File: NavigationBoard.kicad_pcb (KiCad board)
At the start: 2 copper layers, 50 x 45 mm, 49 parts, among them J1 Conn_01x03, J2 Conn_01x03, J3 Conn_01x03, J4 Conn_01x03, J5 USB_C_Receptacle_USB2.0, J6 AVR-ISP-6, J7 Conn_01x02, SW1 SW_Push, U1 ATmega2560-16AU, U2 RFM96W-433S2, U3 FT230XQ, U4 MPL3115A2, U5 ublox_SAM-M8Q, U6 LMZM23600V3, Y1 16MHz

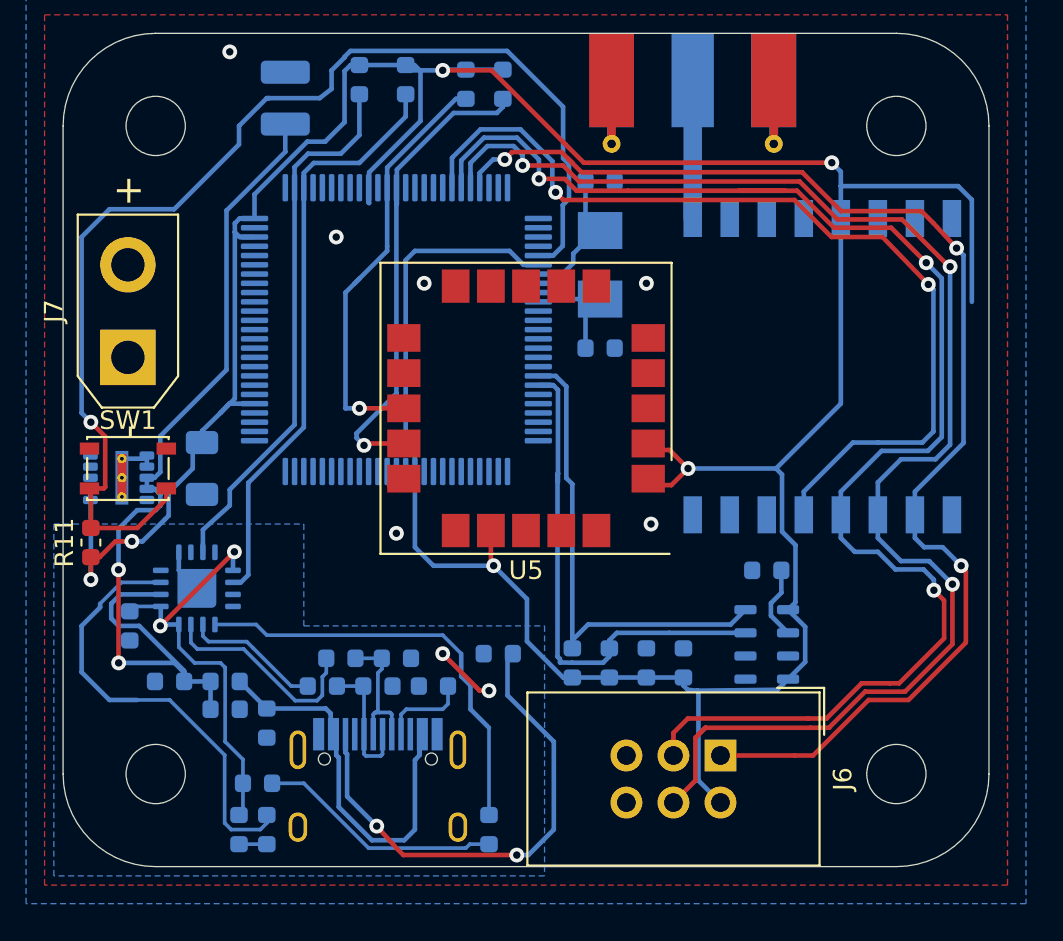
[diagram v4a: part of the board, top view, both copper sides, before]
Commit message: Kleinerer AVR-ISP Stecker
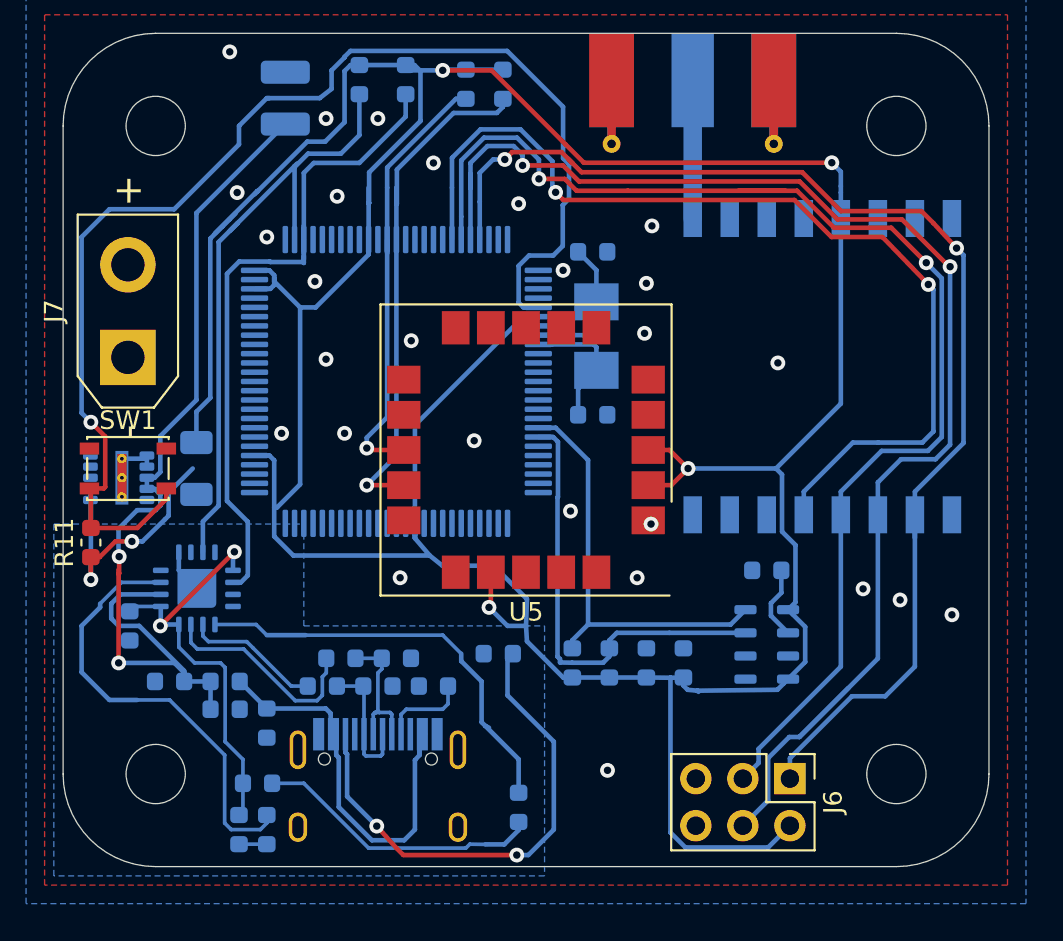
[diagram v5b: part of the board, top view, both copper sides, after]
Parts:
- J6: footprint Connector_IDC:IDC-Header_2x03_P2.54mm_Vertical -> Connector_PinHeader_2.54mm:PinHeader_2x03_P2.54mm_Vertical
- moved J6 3.95 mm to (39.2, 40.2)
- moved Y1 3.86 mm to (28.8, 16.4)
- moved C8 3.82 mm to (28.6, 11.8)
- moved C7 3.62 mm to (28.6, 20.6)
- moved U1 2.80 mm to (18.0, 18.8)
- moved U5 2.25 mm to (25.0, 22.5)
- moved D2 2.00 mm to (24.6, 41.8)
- moved C10 0.30 mm to (7.20, 23.5)
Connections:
- J1 pad 1: Net-(J1-Pad1) -> (no net)
- J1 pad 2: Net-(J1-Pad2) -> (no net)
- J1 pad 3: Net-(J1-Pad3) -> (no net)
- J2 pad 1: Net-(J2-Pad1) -> (no net)
- J2 pad 2: Net-(J2-Pad2) -> (no net)
- J2 pad 3: Net-(J2-Pad3) -> (no net)
- J3 pad 1: Net-(J3-Pad1) -> (no net)
- J3 pad 2: Net-(J3-Pad2) -> (no net)
- J3 pad 3: Net-(J3-Pad3) -> (no net)
- J4 pad 1: Net-(J4-Pad1) -> (no net)
- J4 pad 2: Net-(J4-Pad2) -> (no net)
- J4 pad 3: Net-(J4-Pad3) -> (no net)
- J5 pad A8: Net-(J5-PadA8) -> (no net)
- J5 pad B8: Net-(J5-PadB8) -> (no net)
- J6 pad 5: /~RST -> (no net)
- J7 pad 1: Net-(J7-Pad1) -> (no net)
- J7 pad 2: Net-(J7-Pad2) -> (no net)
- U1 pad 1: Net-(U1-Pad1) -> (no net)
- U1 pad 14: Net-(U1-Pad14) -> (no net)
- U1 pad 15: Net-(U1-Pad15) -> (no net)
- U1 pad 16: Net-(U1-Pad16) -> (no net)
- U1 pad 17: Net-(U1-Pad17) -> (no net)
- U1 pad 18: Net-(U1-Pad18) -> (no net)
- U1 pad 23: Net-(U1-Pad23) -> (no net)
- U1 pad 24: Net-(U1-Pad24) -> (no net)
- U1 pad 25: Net-(U1-Pad25) -> (no net)
- U1 pad 26: Net-(U1-Pad26) -> (no net)
- U1 pad 27: Net-(U1-Pad27) -> (no net)
- U1 pad 28: Net-(U1-Pad28) -> (no net)
- U1 pad 29: Net-(U1-Pad29) -> (no net)
- U1 pad 35: Net-(U1-Pad35) -> (no net)
- U1 pad 36: Net-(U1-Pad36) -> (no net)
- U1 pad 37: Net-(U1-Pad37) -> (no net)
- U1 pad 38: Net-(U1-Pad38) -> (no net)
- U1 pad 39: Net-(U1-Pad39) -> (no net)
- U1 pad 4: Net-(U1-Pad4) -> (no net)
- U1 pad 40: Net-(U1-Pad40) -> (no net)
- U1 pad 41: Net-(U1-Pad41) -> (no net)
- U1 pad 42: Net-(U1-Pad42) -> (no net)
- U1 pad 45: Net-(U1-Pad45) -> (no net)
- U1 pad 46: Net-(U1-Pad46) -> (no net)
- U1 pad 47: Net-(U1-Pad47) -> (no net)
- U1 pad 48: Net-(U1-Pad48) -> (no net)
- U1 pad 49: Net-(U1-Pad49) -> (no net)
- U1 pad 5: Net-(U1-Pad5) -> (no net)
- U1 pad 50: Net-(U1-Pad50) -> (no net)
- U1 pad 51: Net-(U1-Pad51) -> (no net)
- U1 pad 52: Net-(U1-Pad52) -> (no net)
- U1 pad 53: Net-(U1-Pad53) -> (no net)
- U1 pad 54: Net-(U1-Pad54) -> (no net)
- U1 pad 55: Net-(U1-Pad55) -> (no net)
- U1 pad 56: Net-(U1-Pad56) -> (no net)
- U1 pad 57: Net-(U1-Pad57) -> (no net)
- U1 pad 58: Net-(U1-Pad58) -> (no net)
- U1 pad 59: Net-(U1-Pad59) -> (no net)
- U1 pad 6: Net-(U1-Pad6) -> (no net)
- U1 pad 60: Net-(U1-Pad60) -> (no net)
- U1 pad 63: Net-(U1-Pad63) -> (no net)
- U1 pad 64: Net-(U1-Pad64) -> (no net)
- U1 pad 65: Net-(U1-Pad65) -> (no net)
- U1 pad 66: Net-(U1-Pad66) -> (no net)
- U1 pad 67: Net-(U1-Pad67) -> (no net)
- U1 pad 68: Net-(U1-Pad68) -> (no net)
- U1 pad 69: Net-(U1-Pad69) -> (no net)
- U1 pad 7: Net-(U1-Pad7) -> (no net)
- U1 pad 70: Net-(U1-Pad70) -> (no net)
- U1 pad 71: Net-(U1-Pad71) -> (no net)
- U1 pad 72: Net-(U1-Pad72) -> (no net)
- U1 pad 73: Net-(U1-Pad73) -> (no net)
- U1 pad 74: Net-(U1-Pad74) -> (no net)
- U1 pad 75: Net-(U1-Pad75) -> (no net)
- U1 pad 76: Net-(U1-Pad76) -> (no net)
- U1 pad 77: Net-(U1-Pad77) -> (no net)
- U1 pad 78: Net-(U1-Pad78) -> (no net)
- U1 pad 79: Net-(U1-Pad79) -> (no net)
- U1 pad 8: Net-(U1-Pad8) -> (no net)
- U1 pad 82: Net-(U1-Pad82) -> (no net)
- U1 pad 83: Net-(U1-Pad83) -> (no net)
- U1 pad 84: Net-(U1-Pad84) -> (no net)
- U1 pad 85: Net-(U1-Pad85) -> (no net)
- U1 pad 86: Net-(U1-Pad86) -> (no net)
- U1 pad 87: Net-(U1-Pad87) -> (no net)
- U1 pad 88: Net-(U1-Pad88) -> (no net)
- U1 pad 89: Net-(U1-Pad89) -> (no net)
- U1 pad 9: Net-(U1-Pad9) -> (no net)
- U1 pad 90: Net-(U1-Pad90) -> (no net)
- U1 pad 91: Net-(U1-Pad91) -> (no net)
- U1 pad 92: Net-(U1-Pad92) -> (no net)
- U1 pad 93: Net-(U1-Pad93) -> (no net)
- U1 pad 94: Net-(U1-Pad94) -> (no net)
- U1 pad 95: Net-(U1-Pad95) -> (no net)
- U1 pad 96: Net-(U1-Pad96) -> (no net)
- U1 pad 97: Net-(U1-Pad97) -> (no net)
- U2 pad 11: Net-(U2-Pad11) -> (no net)
- U2 pad 12: Net-(U2-Pad12) -> (no net)
- U2 pad 14: Net-(U2-Pad14) -> (no net)
- U2 pad 15: Net-(U2-Pad15) -> (no net)
- U2 pad 16: Net-(U2-Pad16) -> (no net)
- U2 pad 6: Net-(U2-Pad6) -> (no net)
- U2 pad 7: Net-(U2-Pad7) -> (no net)
- U3 pad 12: Net-(U3-Pad12) -> (no net)
- U3 pad 14: Net-(U3-Pad14) -> (no net)
- U3 pad 16: Net-(U3-Pad16) -> (no net)
- U3 pad 4: Net-(U3-Pad4) -> (no net)
- U4 pad 5: Net-(U4-Pad5) -> (no net)
- U4 pad 6: Net-(U4-Pad6) -> (no net)
- U5 pad 12: Net-(U5-Pad12) -> (no net)
- U5 pad 18: Net-(U5-Pad18) -> (no net)
- U5 pad 19: Net-(U5-Pad19) -> (no net)
- U5 pad 7: Net-(U5-Pad7) -> (no net)
- U5 pad 8: Net-(U5-Pad8) -> (no net)
- U5 pad 9: Net-(U5-Pad9) -> (no net)
- U6 pad 10: Net-(U6-Pad10) -> (no net)
- U6 pad 5: Net-(U6-Pad5) -> (no net)
- U6 pad 8: Net-(U6-Pad8) -> (no net)
- U6 pad 9: Net-(U6-Pad9) -> (no net)
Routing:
- net +3V3: track 196.9 -> 224.2 mm
- net /SCK: track 79.2 -> 69.9 mm, vias 3 -> 2
- net /RXD0: track 29.3 -> 34.1 mm
- net /~RESET: track 64.4 -> 68.8 mm
- net /SDA: track 28.4 -> 24.3 mm
- net /SCL: track 26.5 -> 22.8 mm
- net /MOSI: track 77.5 -> 74.2 mm, vias 3 -> 2
- net GNDS: track 5.74 -> 2.41 mm, vias 2 -> 0
- net /TXD0: track 31.9 -> 35.2 mm
- net /~SS: track 50.3 -> 53.1 mm
- net Net-(D2-Pad2): track 13.3 -> 15.8 mm
- net /MISO: track 69.6 -> 67.3 mm, vias 3 -> 2
- net Net-(D2-Pad1): track 23.3 -> 25.1 mm
- net /RXD2: track 23.2 -> 24.6 mm
- net Net-(C8-Pad1): track 7.80 -> 8.84 mm
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
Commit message: Layout weiter gemacht
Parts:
- moved R8 0.32 mm to (18.4, 2.80)
- moved R7 0.30 mm to (16.0, 2.80)
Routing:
- net +3V3: track 224.2 -> 240.0 mm, vias 6 -> 8
- net /RXD0: track 34.1 -> 39.0 mm
- net /SCK: track 69.9 -> 74.0 mm
- net /~RESET: track 68.8 -> 65.9 mm
- net /~SS: track 53.1 -> 55.9 mm
- net /TXD2: track 29.0 -> 27.8 mm
- net /MOSI: track 74.2 -> 73.0 mm
- net /TXD0: track 35.2 -> 36.1 mm
- net /SDA: track 24.3 -> 23.7 mm
- net GND: vias 27 -> 24

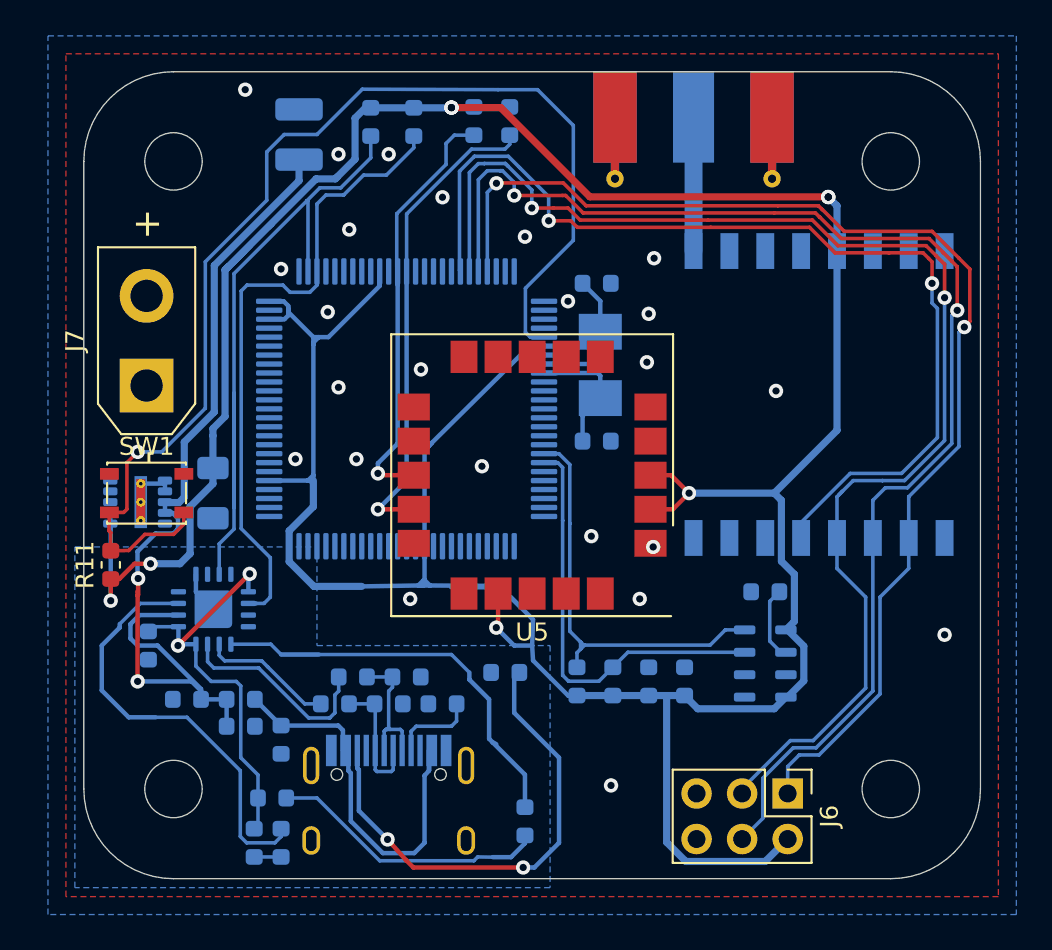
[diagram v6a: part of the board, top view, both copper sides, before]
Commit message: Weniger Leiterbahnen auf der Oberseite
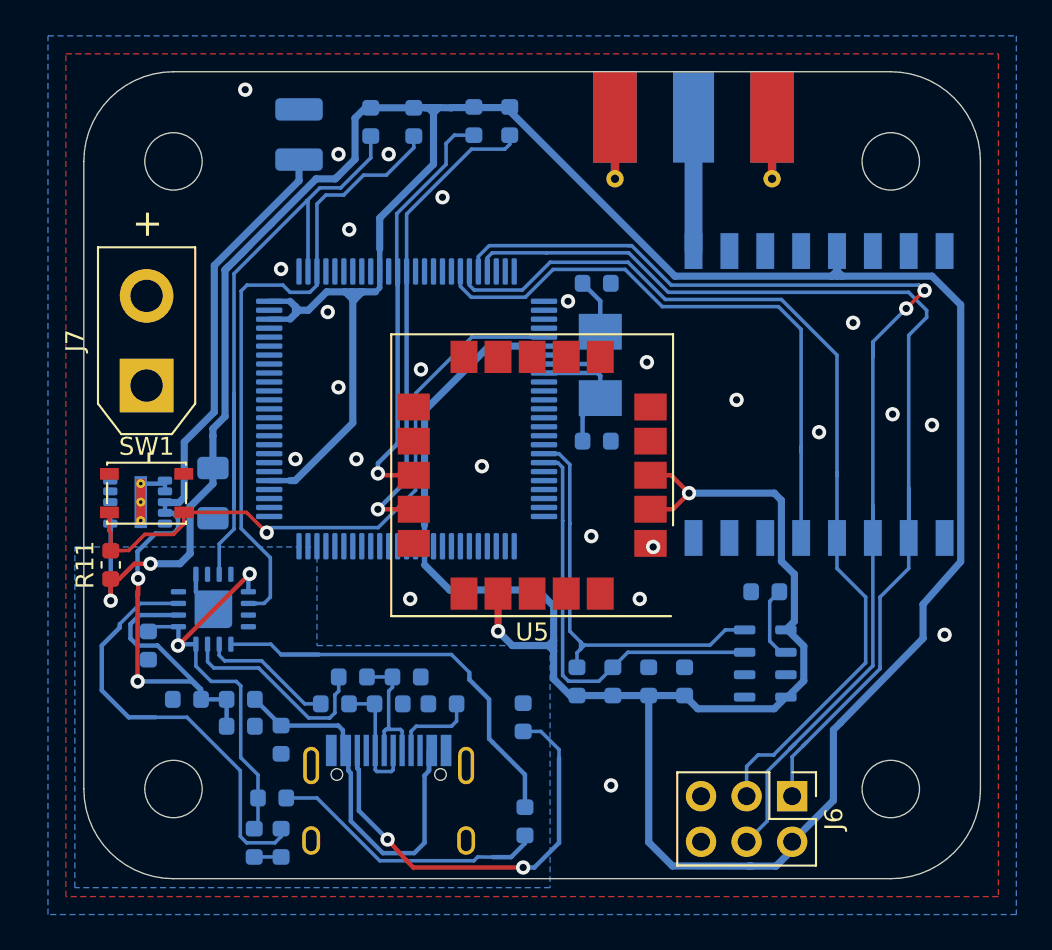
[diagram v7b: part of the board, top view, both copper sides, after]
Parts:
- moved R2 2.69 mm to (24.5, 36.0), turned to 270 degrees
- moved J6 0.29 mm to (39.5, 40.4)
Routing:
- net /~RESET: track 65.9 -> 36.6 mm
- net /~SS: track 55.9 -> 35.0 mm, vias 2 -> 0
- net +3V3: track 240.0 -> 260.4 mm, vias 8 -> 4
- net /SCK: track 74.0 -> 54.0 mm, vias 2 -> 0
- net /MOSI: track 73.0 -> 64.9 mm
- net /MISO: track 67.8 -> 60.1 mm, vias 2 -> 0
- net Net-(J5-PadB5): track 27.1 -> 24.1 mm
- net GND: vias 24 -> 25

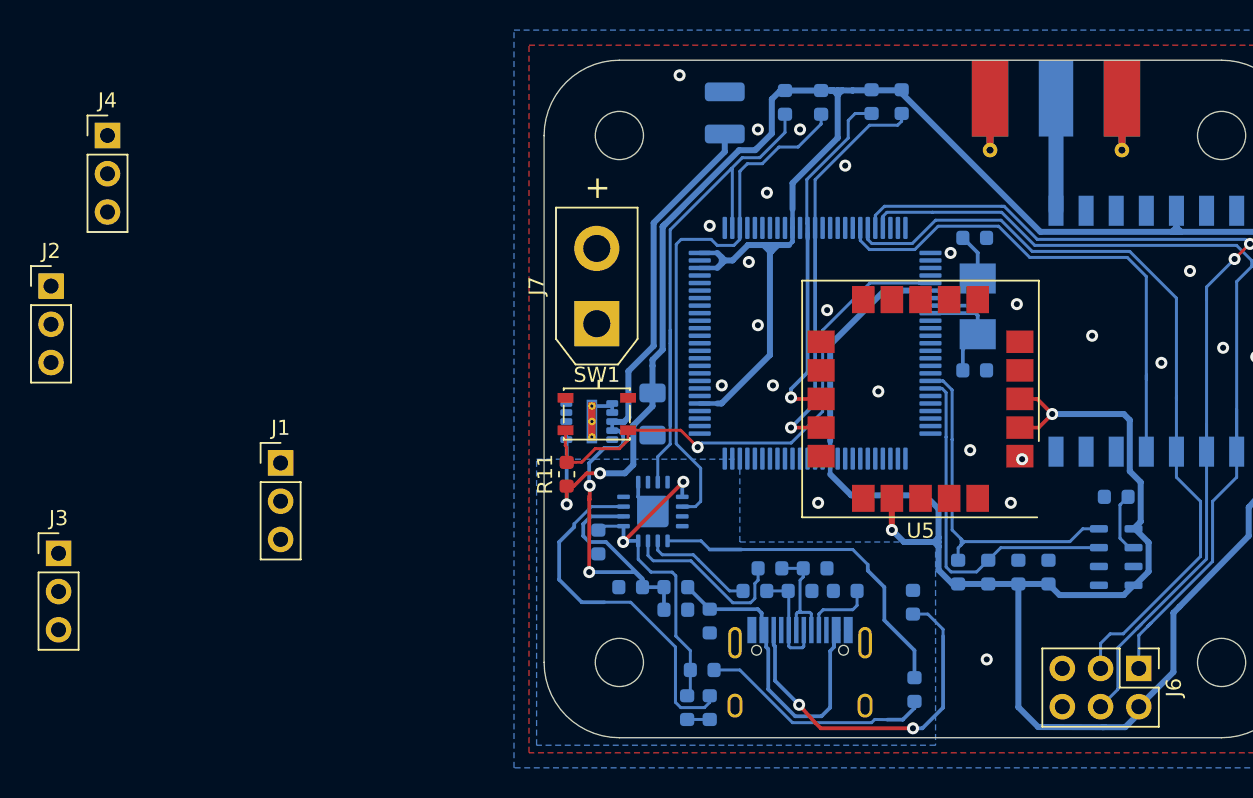
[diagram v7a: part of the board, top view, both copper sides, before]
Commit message: XT 30 entfernt
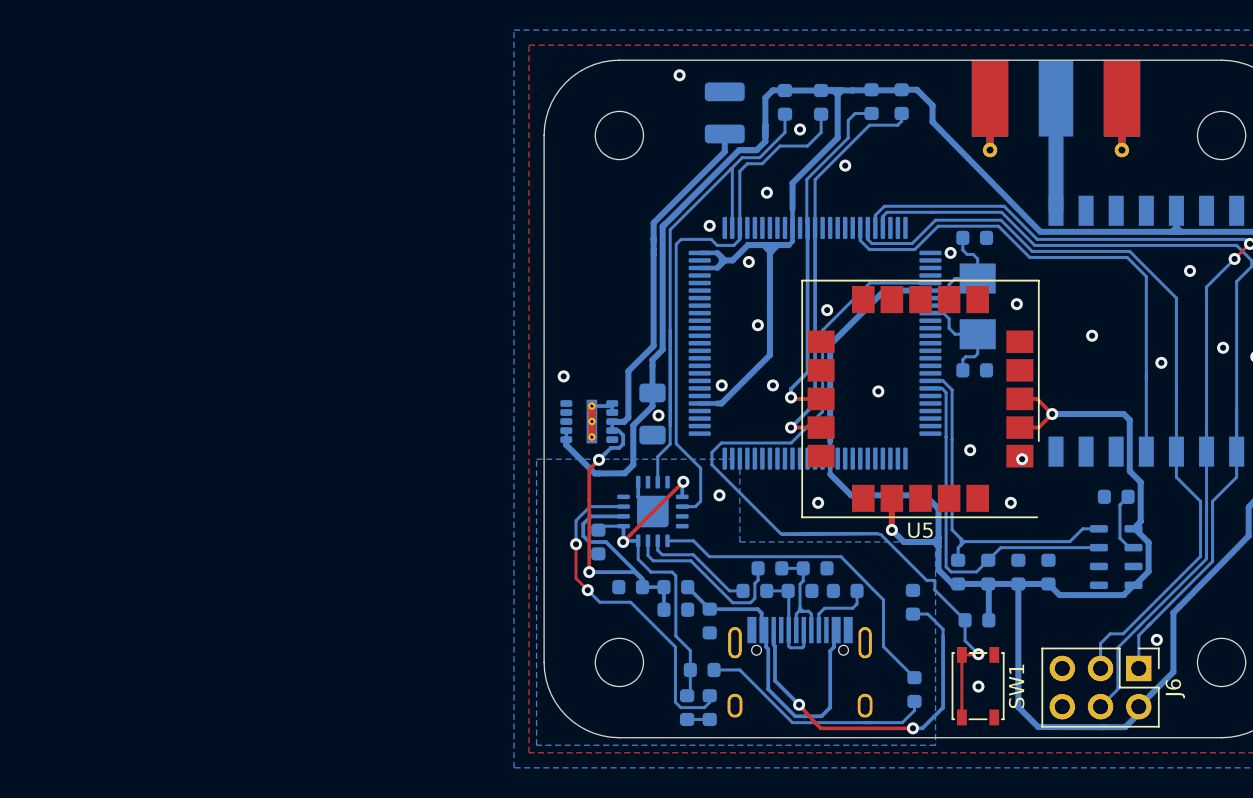
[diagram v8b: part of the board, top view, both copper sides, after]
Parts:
- removed J1, J2, J3, J4: Conn_01x03, Connector_PinHeader_2.54mm:PinHeader_1x03_P2.54mm_Vertical
- removed J7: Conn_01x02, Connector_AMASS:AMASS_XT30UPB-M_1x02_P5.0mm_Vertical
- R11: moved to B.Cu
- moved SW1 31.1 mm to (28.8, 41.6), turned to 270 degrees
- moved R11 28.9 mm to (28.8, 37.2), turned to 180 degrees
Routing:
- net /~RESET: track 36.6 -> 59.8 mm
- net Net-(D2-Pad1): track 24.8 -> 22.0 mm
- net Net-(D1-Pad1): track 24.1 -> 22.5 mm, vias 0 -> 2
- net Net-(C7-Pad1): track 7.26 -> 7.98 mm
- net +3V3: track 260.4 -> 260.5 mm, vias 4 -> 2
- net GND: vias 25 -> 28
